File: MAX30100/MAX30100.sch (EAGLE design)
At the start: 2 parts

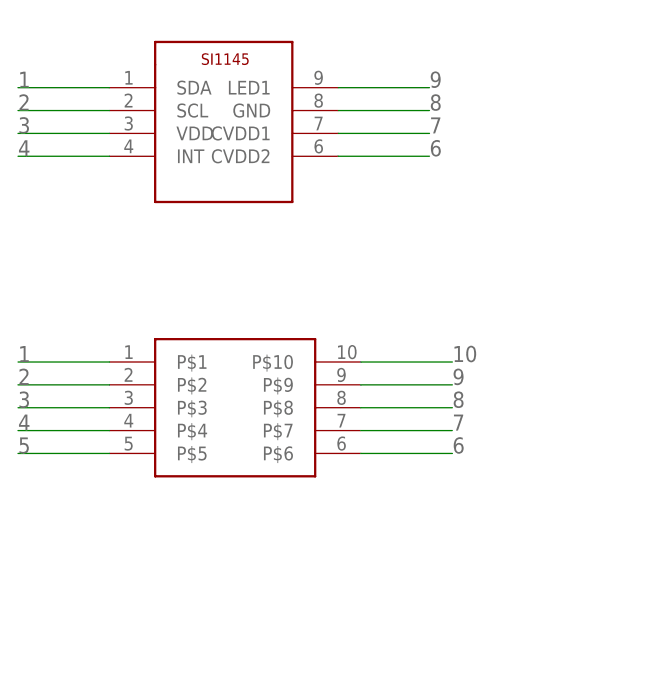
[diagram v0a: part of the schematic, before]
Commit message: Add breakout board
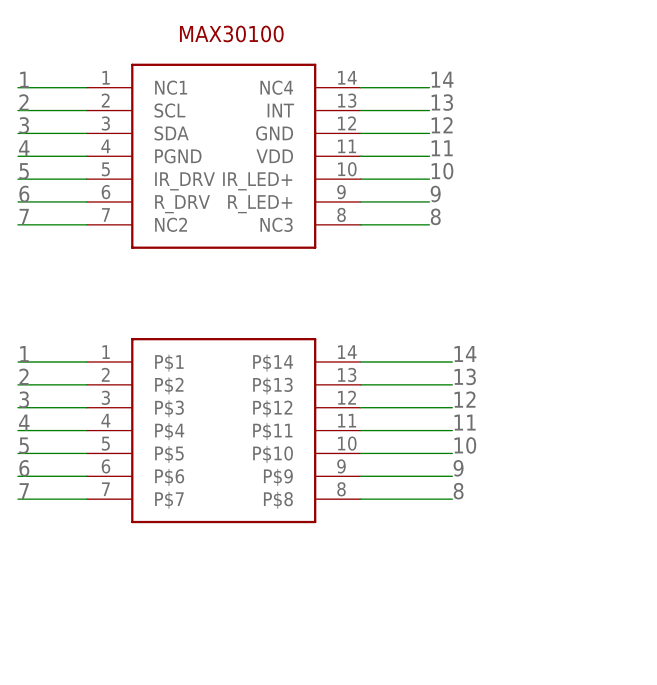
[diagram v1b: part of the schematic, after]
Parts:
- removed SI1145: SL-SI1145, FaBo-Mems:SL-SI1145
- added MAX30100: MA-MAX30100, FaBo-Mems:MA-MAX30100
- U$2: value 10PIN -> 14PIN; device FaBo-Breakout:10PIN -> FaBo-Breakout:14PIN
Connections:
- new net 11: MAX30100.VDD, U$2.P$11
- new net 12: MAX30100.GND, U$2.P$12
- new net 13: MAX30100.INT, U$2.P$13
- new net 14: MAX30100.NC4, U$2.P$14
- net 1: now also MAX30100.NC1; no longer SI1145.SDA
- net 10: now also MAX30100.IR_LED+
- net 2: now also MAX30100.SCL; no longer SI1145.SCL
- net 3: now also MAX30100.SDA; no longer SI1145.VDD
- net 4: now also MAX30100.PGND; no longer SI1145.INT
- net 5: now also MAX30100.IR_DRV
- net 6: now also MAX30100.R_DRV; no longer SI1145.CVDD2
- net 7: now also MAX30100.NC2; no longer SI1145.CVDD1
- net 8: now also MAX30100.NC3; no longer SI1145.GND
- net 9: now also MAX30100.R_LED+; no longer SI1145.LED1
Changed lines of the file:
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@@
 <parts>
 <part name="U$1" library="GClue" deviceset="A4L-LOC" device=""/>
-<part name="SI1145" library="FaBo-Mems" deviceset="SL-SI1145" device=""/>
-<part name="U$2" library="FaBo-Breakout" deviceset="10PIN" device=""/>
+<part name="U$2" library="FaBo-Breakout" deviceset="14PIN" device=""/>
+<part name="MAX30100" library="FaBo-Mems" deviceset="MA-MAX30100" device=""/>
 </parts>
 <sheets>
@@
 <instances>
 <instance part="U$1" gate="G$1" x="0" y="0"/>
-<instance part="SI1145" gate="G$1" x="76.2" y="134.62"/>
-<instance part="U$2" gate="G$1" x="78.74" y="99.06"/>
+<instance part="U$2" gate="G$1" x="76.2" y="99.06"/>
+<instance part="MAX30100" gate="G$1" x="76.2" y="132.08"/>
 </instances>
 <busses>
@@
 <net name="1" class="0">
 <segment>
-<pinref part="SI1145" gate="G$1" pin="SDA"/>
-<wire x1="63.5" y1="139.7" x2="53.34" y2="139.7" width="0.1524" layer="91"/>
 <label x="53.34" y="139.7" size="1.778" layer="95"/>
+<wire x1="60.96" y1="139.7" x2="53.34" y2="139.7" width="0.1524" layer="91"/>
+<pinref part="MAX30100" gate="G$1" pin="NC1"/>
 </segment>
 <segment>
+<label x="53.34" y="109.22" size="1.778" layer="95"/>
 <pinref part="U$2" gate="G$1" pin="P$1"/>
-<wire x1="63.5" y1="109.22" x2="53.34" y2="109.22" width="0.1524" layer="91"/>
-<label x="53.34" y="109.22" size="1.778" layer="95"/>
+<wire x1="60.96" y1="109.22" x2="53.34" y2="109.22" width="0.1524" layer="91"/>
 </segment>
 </net>
 <net name="2" class="0">
 <segment>
-<pinref part="SI1145" gate="G$1" pin="SCL"/>
-<wire x1="63.5" y1="137.16" x2="53.34" y2="137.16" width="0.1524" layer="91"/>
 <label x="53.34" y="137.16" size="1.778" layer="95"/>
+<wire x1="60.96" y1="137.16" x2="53.34" y2="137.16" width="0.1524" layer="91"/>
+<pinref part="MAX30100" gate="G$1" pin="SCL"/>
 </segment>
 <segment>
+<label x="53.34" y="106.68" size="1.778" layer="95"/>
 <pinref part="U$2" gate="G$1" pin="P$2"/>
-<wire x1="63.5" y1="106.68" x2="53.34" y2="106.68" width="0.1524" layer="91"/>
-<label x="53.34" y="106.68" size="1.778" layer="95"/>
+<wire x1="60.96" y1="106.68" x2="53.34" y2="106.68" width="0.1524" layer="91"/>
 </segment>
 </net>
 <net name="3" class="0">
 <segment>
-<pinref part="SI1145" gate="G$1" pin="VDD"/>
-<wire x1="63.5" y1="134.62" x2="53.34" y2="134.62" width="0.1524" layer="91"/>
 <label x="53.34" y="134.62" size="1.778" layer="95"/>
+<wire x1="60.96" y1="134.62" x2="53.34" y2="134.62" width="0.1524" layer="91"/>
+<pinref part="MAX30100" gate="G$1" pin="SDA"/>
 </segment>
 <segment>
+<label x="53.34" y="104.14" size="1.778" layer="95"/>
 <pinref part="U$2" gate="G$1" pin="P$3"/>
-<wire x1="63.5" y1="104.14" x2="53.34" y2="104.14" width="0.1524" layer="91"/>
-<label x="53.34" y="104.14" size="1.778" layer="95"/>
+<wire x1="60.96" y1="104.14" x2="53.34" y2="104.14" width="0.1524" layer="91"/>
 </segment>
 </net>
 <net name="4" class="0">
 <segment>
-<pinref part="SI1145" gate="G$1" pin="INT"/>
-<wire x1="63.5" y1="132.08" x2="53.34" y2="132.08" width="0.1524" layer="91"/>
 <label x="53.34" y="132.08" size="1.778" layer="95"/>
+<wire x1="60.96" y1="132.08" x2="53.34" y2="132.08" width="0.1524" layer="91"/>
+<pinref part="MAX30100" gate="G$1" pin="PGND"/>
 </segment>
 <segment>
+<label x="53.34" y="101.6" size="1.778" layer="95"/>
 <pinref part="U$2" gate="G$1" pin="P$4"/>
-<wire x1="63.5" y1="101.6" x2="53.34" y2="101.6" width="0.1524" layer="91"/>
-<label x="53.34" y="101.6" size="1.778" layer="95"/>
+<wire x1="60.96" y1="101.6" x2="53.34" y2="101.6" width="0.1524" layer="91"/>
 </segment>
 </net>
 <net name="9" class="0">
 <segment>
-<pinref part="SI1145" gate="G$1" pin="LED1"/>
-<wire x1="88.9" y1="139.7" x2="99.06" y2="139.7" width="0.1524" layer="91"/>
-<label x="99.06" y="139.7" size="1.778" layer="95"/>
+<pinref part="U$2" gate="G$1" pin="P$9"/>
+<wire x1="91.44" y1="96.52" x2="101.6" y2="96.52" width="0.1524" layer="91"/>
+<label x="101.6" y="96.52" size="1.778" layer="95"/>
 </segment>
 <segment>
-<pinref part="U$2" gate="G$1" pin="P$9"/>
-<wire x1="91.44" y1="106.68" x2="101.6" y2="106.68" width="0.1524" layer="91"/>
-<label x="101.6" y="106.68" size="1.778" layer="95"/>
+<wire x1="91.44" y1="127" x2="99.06" y2="127" width="0.1524" layer="91"/>
+<label x="99.06" y="127" size="1.778" layer="95"/>
+<pinref part="MAX30100" gate="G$1" pin="R_LED+"/>
 </segment>
 </net>
 <net name="8" class="0">
 <segment>
-<pinref part="SI1145" gate="G$1" pin="GND"/>
-<wire x1="88.9" y1="137.16" x2="99.06" y2="137.16" width="0.1524" layer="91"/>
-<label x="99.06" y="137.16" size="1.778" layer="95"/>
+<pinref part="U$2" gate="G$1" pin="P$8"/>
+<wire x1="91.44" y1="93.98" x2="101.6" y2="93.98" width="0.1524" layer="91"/>
+<label x="101.6" y="93.98" size="1.778" layer="95"/>
 </segment>
 <segment>
-<pinref part="U$2" gate="G$1" pin="P$8"/>
-<wire x1="91.44" y1="104.14" x2="101.6" y2="104.14" width="0.1524" layer="91"/>
-<label x="101.6" y="104.14" size="1.778" layer="95"/>
+<wire x1="91.44" y1="124.46" x2="99.06" y2="124.46" width="0.1524" layer="91"/>
+<label x="99.06" y="124.46" size="1.778" layer="95"/>
+<pinref part="MAX30100" gate="G$1" pin="NC3"/>
 </segment>
 </net>
 <net name="7" class="0">
 <segment>
-<pinref part="SI1145" gate="G$1" pin="CVDD1"/>
-<wire x1="88.9" y1="134.62" x2="99.06" y2="134.62" width="0.1524" layer="91"/>
-<label x="99.06" y="134.62" size="1.778" layer="95"/>
+<pinref part="U$2" gate="G$1" pin="P$7"/>
+<wire x1="60.96" y1="93.98" x2="53.34" y2="93.98" width="0.1524" layer="91"/>
+<label x="53.34" y="93.98" size="1.778" layer="95"/>
 </segment>
 <segment>
-<pinref part="U$2" gate="G$1" pin="P$7"/>
-<wire x1="91.44" y1="101.6" x2="101.6" y2="101.6" width="0.1524" layer="91"/>
-<label x="101.6" y="101.6" size="1.778" layer="95"/>
+<wire x1="60.96" y1="124.46" x2="53.34" y2="124.46" width="0.1524" layer="91"/>
+<label x="53.34" y="124.46" size="1.778" layer="95"/>
+<pinref part="MAX30100" gate="G$1" pin="NC2"/>
 </segment>
 </net>
 <net name="6" class="0">
 <segment>
-<pinref part="SI1145" gate="G$1" pin="CVDD2"/>
-<wire x1="88.9" y1="132.08" x2="99.06" y2="132.08" width="0.1524" layer="91"/>
-<label x="99.06" y="132.08" size="1.778" layer="95"/>
+<pinref part="U$2" gate="G$1" pin="P$6"/>
+<wire x1="60.96" y1="96.52" x2="53.34" y2="96.52" width="0.1524" layer="91"/>
+<label x="53.34" y="96.52" size="1.778" layer="95"/>
 </segment>
 <segment>
-<pinref part="U$2" gate="G$1" pin="P$6"/>
-<wire x1="91.44" y1="99.06" x2="101.6" y2="99.06" width="0.1524" layer="91"/>
-<label x="101.6" y="99.06" size="1.778" layer="95"/>
+<wire x1="60.96" y1="127" x2="53.34" y2="127" width="0.1524" layer="91"/>
+<label x="53.34" y="127" size="1.778" layer="95"/>
+<pinref part="MAX30100" gate="G$1" pin="R_DRV"/>
 </segment>
 </net>
 <net name="5" class="0">
 <segment>
+<label x="53.34" y="99.06" size="1.778" layer="95"/>
 <pinref part="U$2" gate="G$1" pin="P$5"/>
-<wire x1="63.5" y1="99.06" x2="53.34" y2="99.06" width="0.1524" layer="91"/>
-<label x="53.34" y="99.06" size="1.778" layer="95"/>
+<wire x1="60.96" y1="99.06" x2="53.34" y2="99.06" width="0.1524" layer="91"/>
+</segment>
+<segment>
+<wire x1="60.96" y1="129.54" x2="53.34" y2="129.54" width="0.1524" layer="91"/>
+<label x="53.34" y="129.54" size="1.778" layer="95"/>
+<pinref part="MAX30100" gate="G$1" pin="IR_DRV"/>
 </segment>
 </net>
 <net name="10" class="0">
 <segment>
+<wire x1="91.44" y1="99.06" x2="101.6" y2="99.06" width="0.1524" layer="91"/>
+<label x="101.6" y="99.06" size="1.778" layer="95"/>
 <pinref part="U$2" gate="G$1" pin="P$10"/>
+</segment>
+<segment>
+<wire x1="91.44" y1="129.54" x2="99.06" y2="129.54" width="0.1524" layer="91"/>
+<label x="99.06" y="129.54" size="1.778" layer="95"/>
+<pinref part="MAX30100" gate="G$1" pin="IR_LED+"/>
+</segment>
+</net>
+<net name="11" class="0">
+<segment>
+<wire x1="91.44" y1="101.6" x2="101.6" y2="101.6" width="0.1524" layer="91"/>
+<label x="101.6" y="101.6" size="1.778" layer="95"/>
+<pinref part="U$2" gate="G$1" pin="P$11"/>
+</segment>
+<segment>
+<label x="99.06" y="132.08" size="1.778" layer="95"/>
+<wire x1="91.44" y1="132.08" x2="99.06" y2="132.08" width="0.1524" layer="91"/>
+<pinref part="MAX30100" gate="G$1" pin="VDD"/>
+</segment>
+</net>
+<net name="12" class="0">
+<segment>
+<wire x1="91.44" y1="104.14" x2="101.6" y2="104.14" width="0.1524" layer="91"/>
+<label x="101.6" y="104.14" size="1.778" layer="95"/>
+<pinref part="U$2" gate="G$1" pin="P$12"/>
+</segment>
+<segment>
+<label x="99.06" y="134.62" size="1.778" layer="95"/>
+<wire x1="91.44" y1="134.62" x2="99.06" y2="134.62" width="0.1524" layer="91"/>
+<pinref part="MAX30100" gate="G$1" pin="GND"/>
+</segment>
+</net>
+<net name="13" class="0">
+<segment>
+<wire x1="91.44" y1="106.68" x2="101.6" y2="106.68" width="0.1524" layer="91"/>
+<label x="101.6" y="106.68" size="1.778" layer="95"/>
+<pinref part="U$2" gate="G$1" pin="P$13"/>
+</segment>
+<segment>
+<label x="99.06" y="137.16" size="1.778" layer="95"/>
+<wire x1="91.44" y1="137.16" x2="99.06" y2="137.16" width="0.1524" layer="91"/>
+<pinref part="MAX30100" gate="G$1" pin="INT"/>
+</segment>
+</net>
+<net name="14" class="0">
+<segment>
 <wire x1="91.44" y1="109.22" x2="101.6" y2="109.22" width="0.1524" layer="91"/>
 <label x="101.6" y="109.22" size="1.778" layer="95"/>
+<pinref part="U$2" gate="G$1" pin="P$14"/>
+</segment>
+<segment>
+<label x="99.06" y="139.7" size="1.778" layer="95"/>
+<wire x1="91.44" y1="139.7" x2="99.06" y2="139.7" width="0.1524" layer="91"/>
+<pinref part="MAX30100" gate="G$1" pin="NC4"/>
 </segment>
 </net>
